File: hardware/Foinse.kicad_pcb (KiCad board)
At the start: 4 copper layers, 60 x 60 mm, 72 parts, among them J1 ESQ-110-X-X-D, J2 XT30PW-M, J4 PJ-002AH, J6 JTAG-10 PIN, U1 STM32F072C8Tx, U15 INA239AIDGSR, U16 INA239AIDGSR, U17 LTC4412xS6, U19 TPS56A37RPAR, U2 TLV70433DBVT, U4 TJA1051T-3, U5 TPS563203

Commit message: hehe
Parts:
- moved C10 74.3 mm to (190.0, 85.5), turned to 90 degrees
- moved C36 68.6 mm to (95.9, 47.4)
- moved R52 68.6 mm to (91.8, 50.2)
- moved R55 68.6 mm to (93.8, 50.2)
- moved R6 68.6 mm to (94.9, 47.4)
- moved C37 68.6 mm to (90.8, 43.8)
- moved C38 68.6 mm to (88.8, 43.8)
- moved C39 68.6 mm to (89.8, 43.8)
- moved C40 68.6 mm to (94.4, 41.7)
- moved C43 68.6 mm to (103.1, 43.7)
- moved C44 68.6 mm to (107.0, 43.7)
- moved C45 68.6 mm to (106.0, 43.7)
- moved C46 68.6 mm to (105.0, 43.7)
- moved L1 68.6 mm to (98.8, 40.0)
- moved R51 68.6 mm to (90.6, 47.5)
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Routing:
- net VBAT: track 12.8 -> 25.0 mm
- net GND: vias 15 -> 53
- net Net-(U19-SW): vias 0 -> 2
- net 5VSERVO_BS: vias 2 -> 1

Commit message: never
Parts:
- moved R51 63.2 mm to (146.3, 77.5)
- moved R58 63.2 mm to (148.9, 77.1)
- moved C36 63.2 mm to (151.5, 77.4)
- moved C40 63.2 mm to (150.0, 71.8)
- moved C41 63.2 mm to (149.0, 78.8)
- moved C42 63.2 mm to (159.7, 73.7)
- moved C43 63.2 mm to (158.7, 73.7)
- moved R52 63.2 mm to (147.4, 80.3)
- moved R55 63.2 mm to (149.4, 80.3)
- moved R56 63.2 mm to (148.4, 80.3)
- moved R6 63.2 mm to (150.5, 77.4)
- moved C37 63.2 mm to (146.4, 73.8)
- moved C38 63.2 mm to (144.4, 73.8)
- moved C39 63.2 mm to (145.4, 73.8)
- moved C44 63.2 mm to (162.6, 73.7)
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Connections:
- D14 pad 1: VBAT_BS -> VBAT_BS?
- J1 pad 01: 5v_SERVO -> 5VSERVO_BS
- J1 pad 02: 5v_SERVO -> 5VSERVO_BS
- MOSFET1 pad 3: VBAT_BS -> VBAT_BS?
- U17 pad 6: VBAT_BS -> VBAT_BS?
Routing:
- net 5VSERVO_BS: track 0.00 -> 21.4 mm, vias 1 -> 2
- net VBAT: track 25.0 -> 41.5 mm, vias 4 -> 5
- net Net-(MOSFET1-G): track 0.00 -> 13.9 mm
- net Net-(MOSFET1-D): track 0.00 -> 13.8 mm
- net GND: track 1.51 -> 3.28 mm, vias 53 -> 88
- net Net-(U19-SW): track 0.00 -> 1.71 mm, vias 2 -> 0
- net CAN_BUS+: track 0.00 -> 1.54 mm
- net Net-(D12-K): track 0.00 -> 1.48 mm
- net Net-(C41-Pad1): track 1.02 -> 2.43 mm
- net Net-(D12-A): track 0.00 -> 1.06 mm
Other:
- board text added: "Foinse v1.0"

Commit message: gonna
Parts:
- removed D10: BAT54C, Package_TO_SOT_SMD:SOT-23
- moved C11 26.1 mm to (138.5, 96.1), turned to 90 degrees
- moved U2 25.3 mm to (140.9, 96.1), turned to -90 degrees
- moved C10 21.6 mm to (141.3, 93.5), turned to 0 degrees
- moved C19 4.87 mm to (136.2, 91.0)
- moved C21 4.87 mm to (136.2, 90.0)
- moved C22 4.87 mm to (140.9, 84.0)
- moved R3 4.87 mm to (139.7, 86.3)
- moved Rb2 4.87 mm to (139.0, 85.0)
- moved C16 4.87 mm to (136.3, 84.0)
- moved C17 4.87 mm to (136.3, 85.0)
- moved C20 4.87 mm to (136.2, 89.0)
- moved Ra2 4.87 mm to (141.0, 85.0)
- moved SRP4020TA-4R7M1 4.87 mm to (133.0, 88.6)
- moved C18 4.87 mm to (139.3, 87.8)
- moved U5 4.87 mm to (137.5, 86.5)
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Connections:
- C10 pad 1: Net-(U2-IN) -> 5VLOGIC
- D9 pad 1: CAN_BUS+ -> CAN_o+
- D9 pad 2: CAN_BUS+- -> CAN_o-
- R1 pad 2: CAN_BUS+- -> CAN_o-
- R2 pad 1: CAN_BUS+ -> CAN_o+
- U1 pad 32: PA_- -> CAN_-
- U1 pad 33: PA_+ -> CAN_+
- U2 pad 2: Net-(U2-IN) -> 5VLOGIC
- U4 pad 1: CAN_TX -> CAN_+
- U4 pad 4: CAN_RX -> CAN_-
- U4 pad 6: CAN_BUS+- -> CAN_o-
- U4 pad 7: CAN_BUS+ -> CAN_o+
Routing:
- net CAN_o+: track 0.00 -> 13.8 mm
- net GND: track 3.28 -> 15.6 mm, vias 88 -> 94
- net CAN_o-: track 0.00 -> 12.2 mm
- net 3.3V: track 0.00 -> 12.1 mm, vias 0 -> 1
- net 5VLOGIC: track 23.6 -> 33.6 mm
- net CAN_+: track 0.00 -> 5.99 mm
- net CAN_-: track 0.00 -> 5.96 mm
- net NRST: track 0.00 -> 2.61 mm
- net Net-(U1-BOOT0): track 0.00 -> 1.62 mm
- net CAN_BUS+: track 1.54 -> 0.00 mm
- net VBAT: track 41.5 -> 41.3 mm, vias 5 -> 4
- net 5V_LOGIC: vias 0 -> 3

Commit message: give
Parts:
- removed C34, C35: 100nF, Capacitor_SMD:C_0402_1005Metric
- removed D14: D_Schottky, Package_TO_SOT_THT:TO-220-3_Vertical
- removed J4: PJ-002AH, Foinse Footprints:PJ-002AH_CUD
- removed R45, R46: 10 mΩ, Resistor_SMD:R_0402_1005Metric
- removed U15, U16: INA239AIDGSR, Foinse Footprints:VSSOP_9AIDGST_TEX
- added C23: 100nF, Capacitor_SMD:C_0402_1005Metric, F.Cu at (146.5, 66.7)
- added C24: 100nF, Capacitor_SMD:C_0402_1005Metric, F.Cu at (170.1, 72.5)
- added C25: 100nf, Capacitor_SMD:C_0402_1005Metric, F.Cu at (140.8, 71.0)
- added C26: 100nf, Capacitor_SMD:C_0402_1005Metric, F.Cu at (140.8, 65.9)
- added D1: SR1020, footprints:TO254P1050X476X2020-3, F.Cu at (126.0, 83.2)
- added J3: PJ-063AH, footprints:CUI_PJ-063AH, F.Cu at (135.0, 74.7)
- added R7: 35kΩ, Resistor_SMD:R_0402_1005Metric, F.Cu at (140.3, 88.6)
- added U6: ACS71240KEXBLT-010B3, footprints:QFN12_ACS711KEXLT-31AB-T_ALM, F.Cu at (146.0, 69.5)
- added U7: ACS71240KEXBLT-010B3, footprints:QFN12_ACS711KEXLT-31AB-T_ALM, F.Cu at (167.5, 72.5)
- R50: value 3.3k Ω -> 3.3kΩ
- moved C9 8.03 mm to (154.6, 85.1), turned to 0 degrees
- moved C8 6.75 mm to (154.6, 86.1), turned to 0 degrees
- moved R6 1.81 mm to (150.5, 79.2)
- moved MOSFET1 0.81 mm to (141.6, 57.5)
- moved D12 0.70 mm to (138.8, 71.1)
- moved R50 0.70 mm to (138.8, 72.2)
- moved U17 0.70 mm to (140.3, 68.5)
- moved C18 0.07 mm to (139.2, 87.8)
- moved C1 0.06 mm to (143.9, 87.8)
- moved C32 0.06 mm to (143.9, 89.8)
- moved C5 0.06 mm to (142.9, 87.8)
- moved C6 0.06 mm to (142.9, 91.8)
- moved C7 0.06 mm to (143.9, 91.8)
- moved R4 0.06 mm to (142.9, 89.8)
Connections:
- net Net-(U19-PG) renamed Fault2
- net Net-(U5-EN) renamed Fault1
- net VBAT renamed pwr
- net VBAT_BS? renamed pwr_s
- C42 pad 1: 5VSERVO_BS -> 5VSERVO_S
- C43 pad 1: 5VSERVO_BS -> 5VSERVO_S
- C44 pad 1: 5VSERVO_BS -> 5VSERVO_S
- C45 pad 1: 5VSERVO_BS -> 5VSERVO_S
- C46 pad 1: 5VSERVO_BS -> 5VSERVO_S
- J1 pad 01: 5VSERVO_BS -> 5VSERVO
- J1 pad 02: 5VSERVO_BS -> 5VSERVO
- J1 pad 05: 5V_LOGIC -> 5VLOGIC
- J1 pad 06: 5V_LOGIC -> 5VLOGIC
- L1 pad 2: 5VSERVO_BS -> 5VSERVO_S
- R55 pad 1: 5VSERVO_BS -> 5VSERVO_S
- U1 pad 13: unconnected-(U1-PA3-Pad13) -> Sense1
- U1 pad 14: unconnected-(U1-PA4-Pad14) -> Sense2
- U1 pad 15: SPI_CLK -> unconnected-(U1-PA5-Pad15)
- U1 pad 16: SPI_MISO -> unconnected-(U1-PA6-Pad16)
- U1 pad 17: SPI_MOSI -> unconnected-(U1-PA7-Pad17)
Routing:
- net 3.3V: track 12.1 -> 147.7 mm, vias 1 -> 10
- net NRST: track 2.61 -> 68.5 mm, vias 0 -> 1
- net 5VLOGIC: track 33.6 -> 97.6 mm, vias 3 -> 9
- net SWCLK3: track 0.00 -> 49.4 mm, vias 0 -> 1
- net SWDIO: track 0.00 -> 44.0 mm, vias 0 -> 1
- net pwr_s: track 0.00 -> 41.3 mm, vias 0 -> 3
- net Sense2: track 0.00 -> 38.3 mm, vias 0 -> 2
- net Sense1: track 0.00 -> 36.8 mm, vias 0 -> 2
- net Fault1: track 1.06 -> 28.3 mm, vias 0 -> 2
- net GND: track 15.6 -> 40.5 mm, vias 94 -> 110
- net Fault2: track 1.90 -> 26.0 mm, vias 0 -> 2
- net 5VSERVO_S: track 0.00 -> 21.5 mm, vias 0 -> 2
- net 5VSERVO_BS: track 21.4 -> 0.00 mm, vias 2 -> 0
- net Net-(D1-Pad1): track 0.00 -> 20.4 mm
- net pwr: track 41.3 -> 24.8 mm, vias 4 -> 5
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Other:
- board text removed: "*"
- board text removed: "?"

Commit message: you
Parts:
- added G***: LOGO, LOGO, F.Cu at (157.0, 96.6)
- added G***: LOGO, LOGO, F.Cu at (158.8, 62.0)
- added G***: LOGO, LOGO, F.Cu at (162.7, 80.2)
- added G***: LOGO, LOGO, F.Cu at (140.0, 77.5)
- added G***: LOGO, LOGO, F.Cu at (128.8, 88.5)
- moved C9 0.87 mm to (153.7, 85.1), turned to 180 degrees
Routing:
- net GND: track 40.5 -> 42.4 mm, vias 110 -> 111

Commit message: up
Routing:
- net Net-(D1-Pad1): track 20.4 -> 19.4 mm
- net GND: vias 111 -> 114

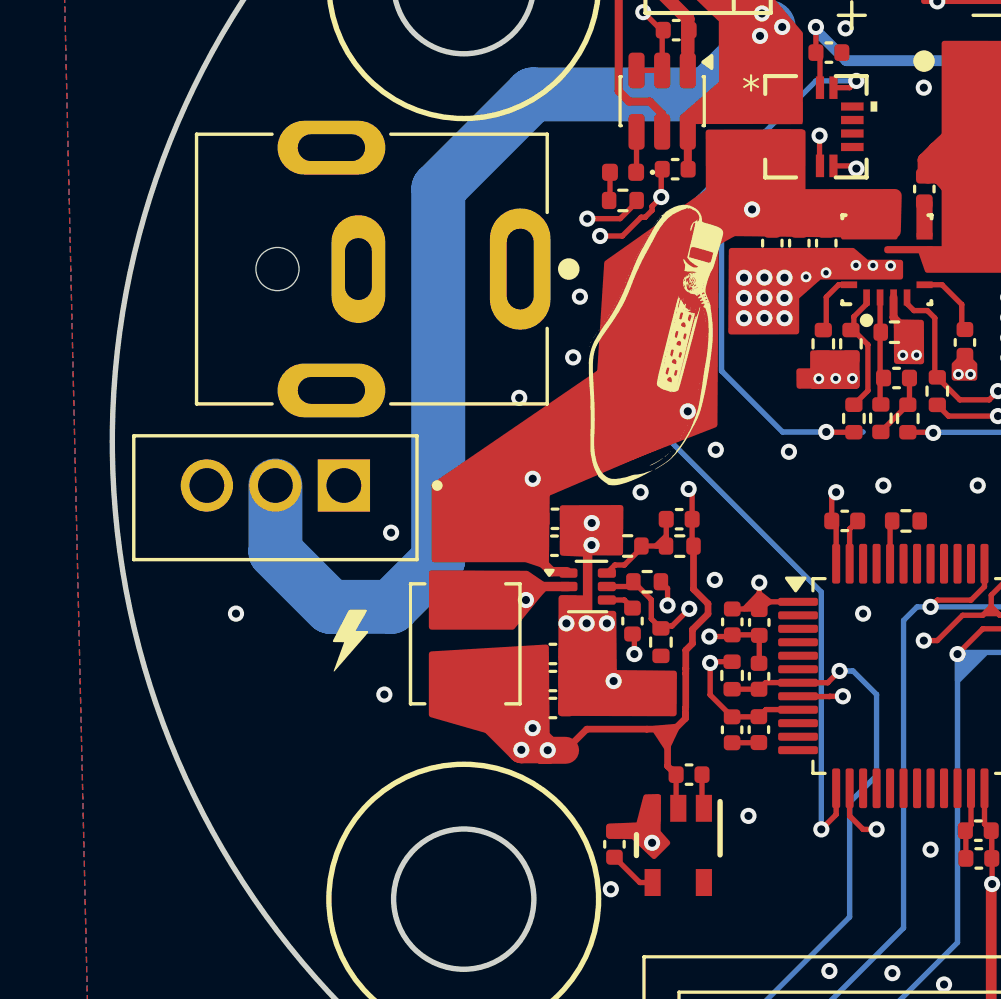
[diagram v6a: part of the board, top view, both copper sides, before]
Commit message: can crystal added
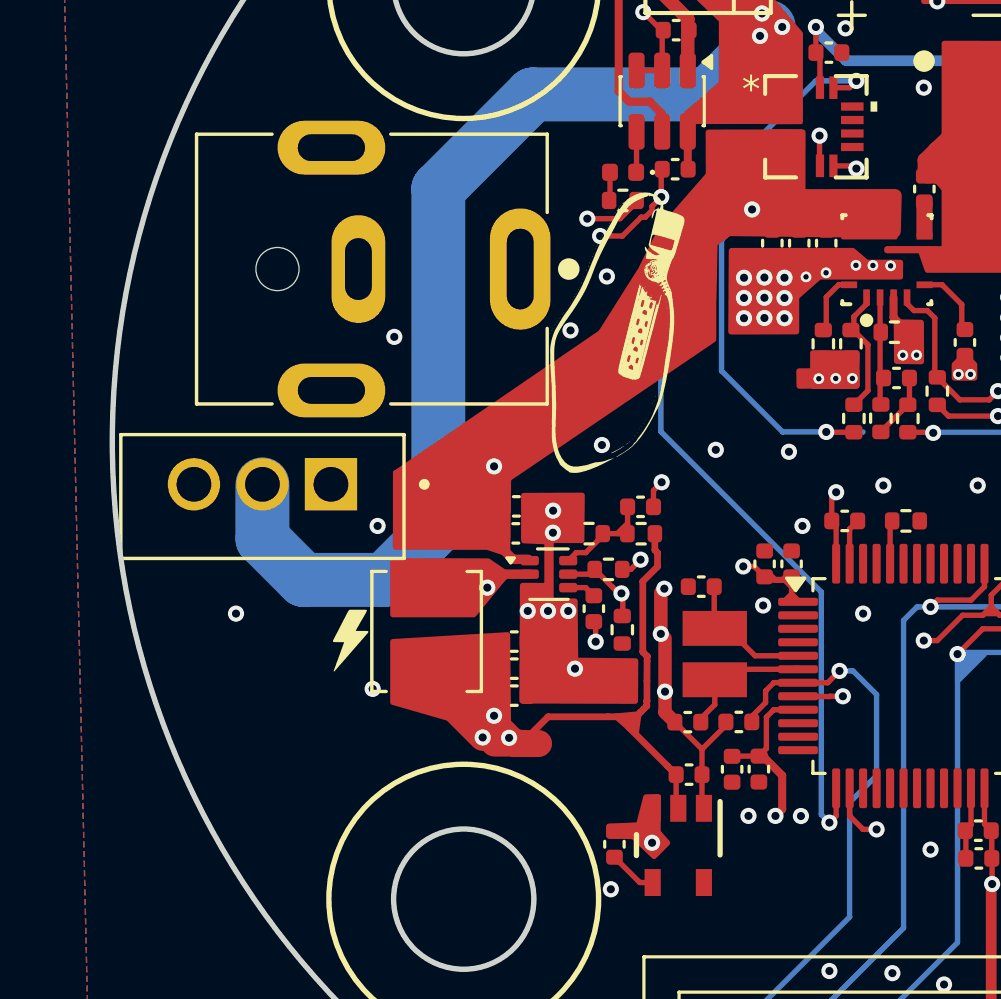
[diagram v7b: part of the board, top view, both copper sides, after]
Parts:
- removed R4: 10kΩ, Resistor_SMD:R_0402_1005Metric
- added C27: 8pF, Capacitor_SMD:C_0402_1005Metric, F.Cu at (141.8, 86.5)
- added C28: 8pF, Capacitor_SMD:C_0402_1005Metric, F.Cu at (141.2, 91.5)
- added XTAL1: NX3225GD-8MHZ-STD-CRA-3, footprints:XTAL_NX3225GD-8MHZ-STD-CRA-3_NDK, F.Cu at (142.2, 89.0)
- moved C1 2.48 mm to (145.1, 85.7), turned to 90 degrees
- moved C5 2.46 mm to (144.1, 85.7), turned to 90 degrees
- moved C32 1.85 mm to (143.1, 91.5), turned to 180 degrees
- moved Rb2 1.50 mm to (137.6, 84.5)
- moved C16 1.50 mm to (134.9, 83.5)
- moved C17 1.50 mm to (134.9, 84.5)
- moved C19 1.50 mm to (134.8, 90.5)
- moved C20 1.50 mm to (134.8, 88.5)
- moved C21 1.50 mm to (134.8, 89.5)
- moved G*** 1.50 mm to (138.6, 77.0)
- moved R3 1.50 mm to (138.3, 85.9)
- moved Ra2 1.50 mm to (139.5, 84.5)
- moved U5 1.50 mm to (136.1, 86.0)
- moved C18 1.50 mm to (137.8, 87.3)
- moved C22 1.50 mm to (139.5, 83.5)
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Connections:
- U1 pad 5: unconnected-(U1-PF0-Pad5) -> Net-(U1-PF0)
- U1 pad 6: unconnected-(U1-PF1-Pad6) -> Net-(U1-PF1)
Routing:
- net 3.3V: track 147.7 -> 138.7 mm
- net Net-(U1-PF0): track 0.00 -> 5.15 mm
- net Net-(U1-PF1): track 0.00 -> 5.15 mm
- net GND: track 42.4 -> 47.4 mm, vias 114 -> 118
- net pwr_s: track 41.3 -> 40.0 mm
- net Net-(D1-Pad1): track 19.4 -> 20.6 mm
- net pwr: track 24.8 -> 23.6 mm, vias 5 -> 4
- net 5VLOGIC: track 97.6 -> 98.2 mm
- net Sense1: track 36.8 -> 36.3 mm

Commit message: minor changes
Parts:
- moved G*** 1.70 mm to (140.2, 77.2)
- moved G*** 0.90 mm to (128.2, 87.8)
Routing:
- net 3.3V: track 138.7 -> 152.2 mm, vias 10 -> 11
- net NRST: track 68.7 -> 69.6 mm
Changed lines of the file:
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@@
 	(footprint "LOGO"
 		(layer "F.Cu")
-		(at 138.567142 77.041082 -14)
+		(at 140.25 77.25 -14)
 		(property "Reference" "G***"
 			(at 0 0 166)
@@
 	(footprint "LOGO"
 		(layer "F.Cu")
-		(at 128.75 88.5)
+		(at 128.25 87.75)
 		(property "Reference" "G***"
 			(at 0 0 0)
@@
 	(gr_poly
 		(pts
+			(xy 143.368896 84.923316) (xy 143.368896 85.673316) (xy 144.118896 85.673316)
+		)
+		(stroke
+			(width 0.2)
+			(type solid)
+		)
+		(fill yes)
+		(layer "In2.Cu")
+		(net 24)
+	)
+	(gr_poly
+		(pts
 			(xy 157.25 90.75) (xy 157.25 92.75) (xy 155.25 92.75)
 		)
@@
 		(net 3)
 	)
+	(gr_poly
+		(pts
+			(xy 143.75 84.5) (xy 143.75 85.5) (xy 143.25 85.25)
+		)
+		(stroke
+			(width 0.2)
+			(type solid)
+		)
+		(fill yes)
+		(layer "In2.Cu")
+		(net 24)
+	)
 	(gr_line
 		(start 171.937477 68.161)
@@
 	)
 	(segment
+		(start 148 90.75)
+		(end 147.584203 91.165797)
+		(width 0.2)
+		(layer "F.Cu")
+		(net 24)
+	)
+	(segment
 		(start 163.655097 91.388021)
 		(end 163.396559 91.646559)
@@
 	)
 	(segment
+		(start 146.75 85.650533)
+		(end 146.75 86.75)
+		(width 0.2)
+		(layer "F.Cu")
+		(net 24)
+	)
+	(segment
 		(start 146.75 84.225533)
 		(end 146.5875 84.063033)
@@
 	)
 	(segment
+		(start 146.75 86.75)
+		(end 146.436967 87.063033)
+		(width 0.2)
+		(layer "F.Cu")
+		(net 24)
+	)
+	(segment
 		(start 152.499416 103.524542)
 		(end 152.499416 106.064542)
@@
 	)
 	(segment
+		(start 146.648293 91.063033)
+		(end 145.3375 91.063033)
+		(width 0.2)
+		(layer "F.Cu")
+		(net 24)
+	)
+	(segment
 		(start 152.532609 96.588387)
 		(end 152.52 96.575778)
@@
 	)
 	(segment
+		(start 146.436967 87.063033)
+		(end 145.3375 87.063033)
+		(width 0.2)
+		(layer "F.Cu")
+		(net 24)
+	)
+	(segment
 		(start 143.711266 85.75)
 		(end 144.195211 86.233945)
@@
 	)
 	(segment
+		(start 146.751057 91.165797)
+		(end 146.648293 91.063033)
+		(width 0.2)
+		(layer "F.Cu")
+		(net 24)
+	)
+	(segment
 		(start 144.75 93.5)
 		(end 144.033003 92.783003)
@@
 	)
 	(segment
+		(start 147.584203 91.165797)
+		(end 146.751057 91.165797)
+		(width 0.2)
+		(layer "F.Cu")
+		(net 24)
+	)
+	(segment
 		(start 146.5875 83.1625)
 		(end 146.75 83)
@@
 	)
 	(via
+		(at 148 90.75)
+		(size 0.6)
+		(drill 0.3)
+		(layers "F.Cu" "B.Cu")
+		(net 24)
+	)
+	(via
 		(at 152.532609 97.525369)
 		(size 0.6)
@@
 	)
 	(segment
+		(start 148 90.75)
+		(end 148 88.75)
+		(width 0.4)
+		(layer "In2.Cu")
+		(net 24)
+	)
+	(segment
 		(start 170.383784 71.116216)
 		(end 157.378994 84.121006)
@@
 	)
 	(segment
+		(start 145 85.75)
+		(end 143.306662 85.75)
+		(width 0.4)
+		(layer "In2.Cu")
+		(net 24)
+	)
+	(segment
 		(start 157.517749 97.525369)
 		(end 152.532609 97.525369)
@@
 	)
 	(segment
+		(start 148 88.75)
+		(end 145 85.75)
+		(width 0.4)
+		(layer "In2.Cu")
+		(net 24)
+	)
+	(segment
 		(start 148.371006 84.121006)
 		(end 147.25 83)
@@
 	)
 	(segment
-		(start 142.5 105.25)
-		(end 143.314542 106.064542)
+		(start 142.5 103.5)
+		(end 142.5 105.25)
 		(width 0.2)
 		(layer "B.Cu")
@@
 	)
 	(segment
-		(start 147.25 94.5)
-		(end 147.25 98.75)
+		(start 146.875 89.625)
+		(end 148.125 89.625)
 		(width 0.2)
 		(layer "B.Cu")
@@
 	)
 	(segment
-		(start 143.314542 106.064542)
-		(end 144.879416 106.064542)
+		(start 148.75 90.25)
+		(end 148.75 93)
 		(width 0.2)
 		(layer "B.Cu")
@@
 	)
 	(segment
-		(start 148.25 90.5)
-		(end 148.25 93.5)
+		(start 143.314542 106.064542)
+		(end 144.879416 106.064542)
 		(width 0.2)
 		(layer "B.Cu")
@@
 	)
 	(segment
-		(start 146.875 89.625)
-		(end 147.375 89.625)
+		(start 147.25 94.5)
+		(end 147.25 98.75)
 		(width 0.2)
 		(layer "B.Cu")
@@
 	)
 	(segment
-		(start 148.25 93.5)
+		(start 148.75 93)
 		(end 147.25 94.5)
 		(width 0.2)
@@
 	)
 	(segment
-		(start 142.5 103.5)
-		(end 142.5 105.25)
+		(start 148.125 89.625)
+		(end 148.75 90.25)
 		(width 0.2)
 		(layer "B.Cu")
@@
 	)
 	(segment
-		(start 147.375 89.625)
-		(end 148.25 90.5)
+		(start 142.5 105.25)
+		(end 143.314542 106.064542)
 		(width 0.2)
 		(layer "B.Cu")
